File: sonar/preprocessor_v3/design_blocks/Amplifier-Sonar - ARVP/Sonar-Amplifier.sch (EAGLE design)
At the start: 20 parts, among them U1 AD8336ACPZ-R7

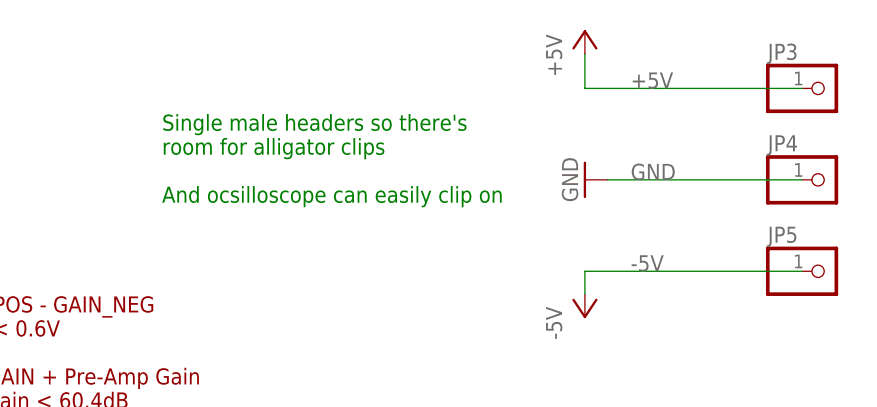
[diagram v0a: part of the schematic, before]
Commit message: Using 0.2" pitch headers
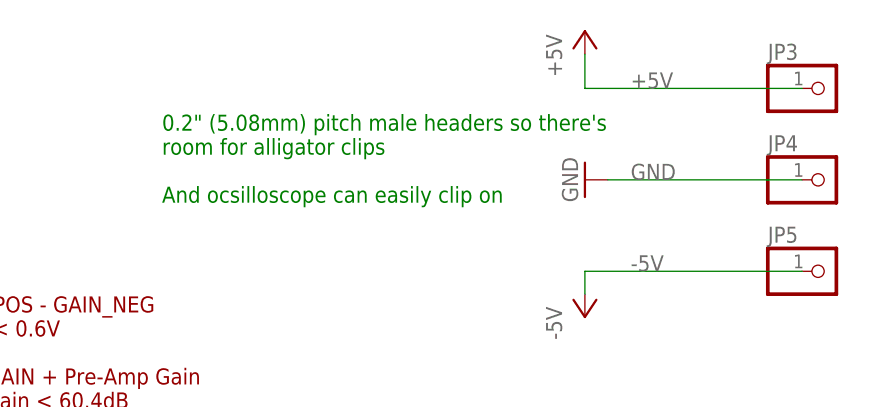
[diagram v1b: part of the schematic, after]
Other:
- note added: "0.2" (5.08mm) pitch male headers so there's room for alligator clips And ocsilloscope can easily clip on"
- note removed: "Single male headers so there's room for alligator clips And ocsilloscope can easily clip on"
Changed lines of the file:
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@@
 <text x="203.2" y="83.82" size="1.778" layer="92">Noise Filter for
 Gain Control</text>
-<text x="162.56" y="177.8" size="1.778" layer="91">Single male headers so there's
+<text x="162.56" y="177.8" size="1.778" layer="91">0.2" (5.08mm) pitch male headers so there's
 room for alligator clips
 And ocsilloscope can easily clip on</text>
